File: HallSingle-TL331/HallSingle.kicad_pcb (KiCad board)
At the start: 2 copper layers, 12 x 23.5 mm, 11 parts, among them J1 Conn_01x03, U1 SS49E, U2 TL331

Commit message: Fixed TL orientation. ( previously fixed an error that was not an error ) thining is hard sometimes.
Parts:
- turned U2 to 0 degrees
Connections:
- U2 pad 1: Net-(C1-Pad1) -> Net-(U1-Pad2)
- U2 pad 3: Net-(U1-Pad2) -> Net-(C1-Pad1)
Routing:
- net Net-(U1-Pad2): track 5.80 -> 2.19 mm
- net Signal: track 32.7 -> 29.7 mm
- net GND: track 6.90 -> 4.70 mm
- net Net-(C1-Pad1): track 7.69 -> 6.98 mm
- net +5V: track 5.17 -> 4.62 mm, vias 3 -> 4
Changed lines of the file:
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@@
     (thickness 1.6)
     (drawings 12)
-    (tracks 58)
+    (tracks 55)
     (zones 0)
     (modules 11)
@@
   )
   (module Package_TO_SOT_SMD:SOT-23-5 (layer F.Cu)
-    (at 147.5 59.55 180)
+    (at 147.5 59.55)
     (descr "5-pin SOT23 package")
     (tags SOT-23-5)
@@
       (effects (font (size 0.5 0.5) (thickness 0.075)))
     )
-    (pad 5 smd rect (at 1.1 -0.95 180) (size 1.06 0.65) (layers F.Cu F.Paste F.Mask)
+    (pad 5 smd rect (at 1.1 -0.95) (size 1.06 0.65) (layers F.Cu F.Paste F.Mask)
       (net 3 +5V))
-    (pad 4 smd rect (at 1.1 0.95 180) (size 1.06 0.65) (layers F.Cu F.Paste F.Mask)
+    (pad 4 smd rect (at 1.1 0.95) (size 1.06 0.65) (layers F.Cu F.Paste F.Mask)
       (net 4 Signal))
-    (pad 3 smd rect (at -1.1 0.95 180) (size 1.06 0.65) (layers F.Cu F.Paste F.Mask)
+    (pad 3 smd rect (at -1.1 0.95) (size 1.06 0.65) (layers F.Cu F.Paste F.Mask)
+      (net 2 "Net-(C1-Pad1)"))
+    (pad 2 smd rect (at -1.1 0) (size 1.06 0.65) (layers F.Cu F.Paste F.Mask)
+      (net 1 GND))
+    (pad 1 smd rect (at -1.1 -0.95) (size 1.06 0.65) (layers F.Cu F.Paste F.Mask)
       (net 6 "Net-(U1-Pad2)"))
-    (pad 2 smd rect (at -1.1 0 180) (size 1.06 0.65) (layers F.Cu F.Paste F.Mask)
-      (net 1 GND))
-    (pad 1 smd rect (at -1.1 -0.95 180) (size 1.06 0.65) (layers F.Cu F.Paste F.Mask)
-      (net 2 "Net-(C1-Pad1)"))
     (model ${KISYS3DMOD}/Package_TO_SOT_SMD.3dshapes/SOT-23-5.wrl
       (at (xyz 0 0 0))
@@
   (gr_line (start 150 58) (end 150 79.5) (layer Edge.Cuts) (width 0.05))
   (gr_line (start 139 57) (end 149 57) (layer Edge.Cuts) (width 0.05))
+  (via (at 145.15 60.55) (size 0.8) (drill 0.4) (layers F.Cu B.Cu) (net 3))
   (segment (start 139.554001 58.946999) (end 139.954 58.547) (width 0.3048) (layer F.Cu) (net 1))
   (segment (start 142.272 59.5605) (end 142.272 59.5605) (width 0.6096) (layer F.Cu) (net 1))
   (segment (start 142.2825 59.55) (end 142.272 59.5605) (width 0.6096) (layer F.Cu) (net 1))
-  (segment (start 148.6 59.55) (end 142.2825 59.55) (width 0.6096) (layer F.Cu) (net 1))
+  (segment (start 146.4 59.55) (end 142.2825 59.55) (width 0.6096) (layer F.Cu) (net 1))
   (segment (start 148.45 62.725) (end 148.463 62.738) (width 0.3048) (layer F.Cu) (net 2))
   (segment (start 147.9885 62.738) (end 148.463 62.738) (width 0.3048) (layer F.Cu) (net 2))
@@
   (segment (start 148.463 62.45) (end 146.7485 62.45) (width 0.3048) (layer F.Cu) (net 2))
   (segment (start 146.558 64.9605) (end 146.558 62.9285) (width 0.3048) (layer F.Cu) (net 2))
+  (segment (start 148.463 60.637) (end 148.6 60.5) (width 0.3048) (layer F.Cu) (net 4))
+  (segment (start 148.6 62.2125) (end 148.45 62.3625) (width 0.3048) (layer F.Cu) (net 2))
   (segment (start 146.4 62.392) (end 146.558 62.55) (width 0.3048) (layer F.Cu) (net 2))
-  (segment (start 148.463 60.637) (end 148.6 60.5) (width 0.3048) (layer F.Cu) (net 2))
-  (segment (start 147.043527 62.064473) (end 146.558 62.55) (width 0.3048) (layer F.Cu) (net 2))
-  (segment (start 148.6 62.2125) (end 148.45 62.3625) (width 0.3048) (layer F.Cu) (net 2))
-  (segment (start 148.6 60.5) (end 148.6 62.2125) (width 0.3048) (layer F.Cu) (net 2))
+  (segment (start 146.4 60.5) (end 146.4 62.392) (width 0.3048) (layer F.Cu) (net 2))
   (via (at 142.15 63.5) (size 0.8) (drill 0.4) (layers F.Cu B.Cu) (net 3))
-  (via (at 145.25 61.05) (size 0.8) (drill 0.4) (layers F.Cu B.Cu) (net 3))
   (segment (start 139.446 62.738) (end 139.446 62.738) (width 0.6096) (layer F.Cu) (net 3))
   (segment (start 139.446 62.738) (end 139.7935 62.738) (width 0.6096) (layer F.Cu) (net 3))
@@
   (segment (start 141.65 63.95) (end 142.15 63.45) (width 0.6096) (layer F.Cu) (net 3))
   (segment (start 141.65 64.2375) (end 141.65 63.95) (width 0.6096) (layer F.Cu) (net 3))
-  (segment (start 145.8 60.5) (end 145.25 61.05) (width 0.6096) (layer F.Cu) (net 3))
-  (segment (start 146.4 60.5) (end 145.8 60.5) (width 0.6096) (layer F.Cu) (net 3))
-  (segment (start 144.7105 60.5105) (end 145.25 61.05) (width 0.6096) (layer F.Cu) (net 3))
-  (segment (start 144.272 60.5105) (end 144.7105 60.5105) (width 0.6096) (layer F.Cu) (net 3))
+  (via (at 147.7 58.05) (size 0.8) (drill 0.4) (layers F.Cu B.Cu) (net 3))
+  (segment (start 148.25 58.6) (end 147.7 58.05) (width 0.6096) (layer F.Cu) (net 3))
+  (segment (start 148.6 58.6) (end 148.25 58.6) (width 0.6096) (layer F.Cu) (net 3))
+  (segment (start 145.1105 60.5105) (end 145.15 60.55) (width 0.6096) (layer F.Cu) (net 3))
+  (segment (start 144.272 60.5105) (end 145.1105 60.5105) (width 0.6096) (layer F.Cu) (net 3))
   (via (at 140.9 61.4) (size 0.8) (drill 0.4) (layers F.Cu B.Cu) (net 4))
   (segment (start 141.65 62.15) (end 140.9 61.4) (width 0.3048) (layer F.Cu) (net 4))
@@
   (segment (start 140 60.5) (end 140.9 61.4) (width 0.3048) (layer F.Cu) (net 4))
   (segment (start 140 60.4375) (end 140 60.5) (width 0.3048) (layer F.Cu) (net 4))
+  (segment (start 148.6 60.5) (end 148.6 60.5) (width 0.3048) (layer F.Cu) (net 4))
+  (via (at 147.7 61.15) (size 0.8) (drill 0.4) (layers F.Cu B.Cu) (net 4))
+  (segment (start 148.35 60.5) (end 147.7 61.15) (width 0.3048) (layer F.Cu) (net 4))
+  (segment (start 148.6 60.5) (end 148.35 60.5) (width 0.3048) (layer F.Cu) (net 4))
+  (segment (start 149.4 62.85) (end 147.7 61.15) (width 0.3048) (layer B.Cu) (net 4))
+  (segment (start 149.399999 76.424291) (end 149.4 62.85) (width 0.3048) (layer B.Cu) (net 4))
+  (segment (start 148 78.58) (end 148 77.82429) (width 0.3048) (layer B.Cu) (net 4))
   (segment (start 148 77.82429) (end 149.399999 76.424291) (width 0.3048) (layer B.Cu) (net 4))
-  (segment (start 148 78.58) (end 148 77.82429) (width 0.3048) (layer B.Cu) (net 4))
-  (segment (start 146.451 58.6105) (end 146.4535 58.608) (width 0.3048) (layer F.Cu) (net 4))
-  (via (at 147.4 58.6) (size 0.8) (drill 0.4) (layers F.Cu B.Cu) (net 4))
-  (segment (start 146.4 58.6) (end 147.4 58.6) (width 0.3048) (layer F.Cu) (net 4))
-  (segment (start 149.399999 60.599999) (end 147.4 58.6) (width 0.3048) (layer B.Cu) (net 4))
-  (segment (start 149.399999 76.424291) (end 149.399999 60.599999) (width 0.3048) (layer B.Cu) (net 4))
-  (segment (start 141.299999 61.000001) (end 140.9 61.4) (width 0.3048) (layer B.Cu) (net 4))
-  (segment (start 146.255601 59.744399) (end 142.555601 59.744399) (width 0.3048) (layer B.Cu) (net 4))
-  (segment (start 142.555601 59.744399) (end 141.299999 61.000001) (width 0.3048) (layer B.Cu) (net 4))
-  (segment (start 147.4 58.6) (end 146.255601 59.744399) (width 0.3048) (layer B.Cu) (net 4))
+  (segment (start 147.300001 61.549999) (end 141.049999 61.549999) (width 0.3048) (layer B.Cu) (net 4))
+  (segment (start 141.049999 61.549999) (end 140.9 61.4) (width 0.3048) (layer B.Cu) (net 4))
+  (segment (start 147.7 61.15) (end 147.300001 61.549999) (width 0.3048) (layer B.Cu) (net 4))
+  (segment (start 146.451 58.6105) (end 146.4535 58.608) (width 0.3048) (layer F.Cu) (net 6))
   (segment (start 143.07763 74) (end 142 74) (width 0.3048) (layer F.Cu) (net 5))
   (segment (start 148.463 64.613) (end 146.794399 66.281601) (width 0.3048) (layer F.Cu) (net 5))
@@
   (segment (start 146.794399 70.283231) (end 143.07763 74) (width 0.3048) (layer F.Cu) (net 5))
   (segment (start 144.5 76.5) (end 142 74) (width 0.3048) (layer F.Cu) (net 5))
+  (segment (start 144.322 58.6105) (end 144.272 58.6105) (width 0.3048) (layer F.Cu) (net 6))
   (segment (start 144.2825 58.6) (end 144.272 58.6105) (width 0.3048) (layer F.Cu) (net 6))
-  (segment (start 144.322 58.6105) (end 144.272 58.6105) (width 0.3048) (layer F.Cu) (net 6))
-  (segment (start 144.272 57.9057) (end 144.272 58.6105) (width 0.3048) (layer F.Cu) (net 6))
-  (segment (start 148.474199 57.844399) (end 144.333301 57.844399) (width 0.3048) (layer F.Cu) (net 6))
-  (segment (start 148.6 57.9702) (end 148.474199 57.844399) (width 0.3048) (layer F.Cu) (net 6))
-  (segment (start 144.333301 57.844399) (end 144.272 57.9057) (width 0.3048) (layer F.Cu) (net 6))
-  (segment (start 148.6 58.6) (end 148.6 57.9702) (width 0.3048) (layer F.Cu) (net 6))
+  (segment (start 146.4 58.6) (end 144.2825 58.6) (width 0.3048) (layer F.Cu) (net 6))
   (zone (net 3) (net_name +5V) (layer B.Cu) (hatch edge 0.508)
     (connect_pads (clearance 0.508))

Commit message: added info to silkscreen
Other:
- board text added: "NC V1.1 TL331"
- board text removed: "NC V1.1"
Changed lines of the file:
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@@
     )
   )
-  (gr_text "NC V1.1\n" (at 139.15 69.05 90) (layer B.SilkS)
+  (gr_text "NC V1.1\nTL331" (at 139.9 69.1 90) (layer B.SilkS)
     (effects (font (size 1 1) (thickness 0.15)) (justify mirror))
   )
@@
   (gr_line (start 150 58) (end 150 79.5) (layer Edge.Cuts) (width 0.05))
   (gr_line (start 139 57) (end 149 57) (layer Edge.Cuts) (width 0.05))
-  (via (at 145.15 60.55) (size 0.8) (drill 0.4) (layers F.Cu B.Cu) (net 3))
   (segment (start 139.554001 58.946999) (end 139.954 58.547) (width 0.3048) (layer F.Cu) (net 1))
   (segment (start 142.272 59.5605) (end 142.272 59.5605) (width 0.6096) (layer F.Cu) (net 1))
@@
   (segment (start 148.463 62.45) (end 146.7485 62.45) (width 0.3048) (layer F.Cu) (net 2))
   (segment (start 146.558 64.9605) (end 146.558 62.9285) (width 0.3048) (layer F.Cu) (net 2))
-  (segment (start 148.463 60.637) (end 148.6 60.5) (width 0.3048) (layer F.Cu) (net 4))
   (segment (start 148.6 62.2125) (end 148.45 62.3625) (width 0.3048) (layer F.Cu) (net 2))
   (segment (start 146.4 62.392) (end 146.558 62.55) (width 0.3048) (layer F.Cu) (net 2))
   (segment (start 146.4 60.5) (end 146.4 62.392) (width 0.3048) (layer F.Cu) (net 2))
+  (via (at 145.15 60.55) (size 0.8) (drill 0.4) (layers F.Cu B.Cu) (net 3))
   (via (at 142.15 63.5) (size 0.8) (drill 0.4) (layers F.Cu B.Cu) (net 3))
   (segment (start 139.446 62.738) (end 139.446 62.738) (width 0.6096) (layer F.Cu) (net 3))
@@
   (segment (start 145.1105 60.5105) (end 145.15 60.55) (width 0.6096) (layer F.Cu) (net 3))
   (segment (start 144.272 60.5105) (end 145.1105 60.5105) (width 0.6096) (layer F.Cu) (net 3))
+  (segment (start 148.463 60.637) (end 148.6 60.5) (width 0.3048) (layer F.Cu) (net 4))
   (via (at 140.9 61.4) (size 0.8) (drill 0.4) (layers F.Cu B.Cu) (net 4))
   (segment (start 141.65 62.15) (end 140.9 61.4) (width 0.3048) (layer F.Cu) (net 4))
@@
   (segment (start 141.049999 61.549999) (end 140.9 61.4) (width 0.3048) (layer B.Cu) (net 4))
   (segment (start 147.7 61.15) (end 147.300001 61.549999) (width 0.3048) (layer B.Cu) (net 4))
-  (segment (start 146.451 58.6105) (end 146.4535 58.608) (width 0.3048) (layer F.Cu) (net 6))
   (segment (start 143.07763 74) (end 142 74) (width 0.3048) (layer F.Cu) (net 5))
   (segment (start 148.463 64.613) (end 146.794399 66.281601) (width 0.3048) (layer F.Cu) (net 5))
@@
   (segment (start 146.794399 70.283231) (end 143.07763 74) (width 0.3048) (layer F.Cu) (net 5))
   (segment (start 144.5 76.5) (end 142 74) (width 0.3048) (layer F.Cu) (net 5))
+  (segment (start 146.451 58.6105) (end 146.4535 58.608) (width 0.3048) (layer F.Cu) (net 6))
   (segment (start 144.322 58.6105) (end 144.272 58.6105) (width 0.3048) (layer F.Cu) (net 6))
   (segment (start 144.2825 58.6) (end 144.272 58.6105) (width 0.3048) (layer F.Cu) (net 6))

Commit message: further fixes and gerbers updated this time
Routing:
- net +5V: track 4.62 -> 4.96 mm, vias 4 -> 3
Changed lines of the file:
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@@
     (thickness 1.6)
     (drawings 12)
-    (tracks 55)
+    (tracks 52)
     (zones 0)
     (modules 11)
@@
   (gr_line (start 150 58) (end 150 79.5) (layer Edge.Cuts) (width 0.05))
   (gr_line (start 139 57) (end 149 57) (layer Edge.Cuts) (width 0.05))
+  (via (at 140.6 63.3) (size 0.8) (drill 0.4) (layers F.Cu B.Cu) (net 3))
   (segment (start 139.554001 58.946999) (end 139.954 58.547) (width 0.3048) (layer F.Cu) (net 1))
   (segment (start 142.272 59.5605) (end 142.272 59.5605) (width 0.6096) (layer F.Cu) (net 1))
@@
   (segment (start 146.4 60.5) (end 146.4 62.392) (width 0.3048) (layer F.Cu) (net 2))
   (via (at 145.15 60.55) (size 0.8) (drill 0.4) (layers F.Cu B.Cu) (net 3))
-  (via (at 142.15 63.5) (size 0.8) (drill 0.4) (layers F.Cu B.Cu) (net 3))
-  (segment (start 139.446 62.738) (end 139.446 62.738) (width 0.6096) (layer F.Cu) (net 3))
-  (segment (start 139.446 62.738) (end 139.7935 62.738) (width 0.6096) (layer F.Cu) (net 3))
-  (via (at 139.05 61.45) (size 0.8) (drill 0.4) (layers F.Cu B.Cu) (net 3))
-  (segment (start 139.6 62) (end 139.05 61.45) (width 0.6096) (layer F.Cu) (net 3))
-  (segment (start 139.6 62.3625) (end 139.6 62) (width 0.6096) (layer F.Cu) (net 3))
   (segment (start 141.65 64.2375) (end 141.6625 64.2375) (width 0.6096) (layer F.Cu) (net 3))
   (segment (start 148 73.5) (end 148 73.6) (width 0.3048) (layer B.Cu) (net 3))
-  (segment (start 141.65 63.95) (end 142.15 63.45) (width 0.6096) (layer F.Cu) (net 3))
-  (segment (start 141.65 64.2375) (end 141.65 63.95) (width 0.6096) (layer F.Cu) (net 3))
   (via (at 147.7 58.05) (size 0.8) (drill 0.4) (layers F.Cu B.Cu) (net 3))
   (segment (start 148.25 58.6) (end 147.7 58.05) (width 0.6096) (layer F.Cu) (net 3))
@@
   (segment (start 145.1105 60.5105) (end 145.15 60.55) (width 0.6096) (layer F.Cu) (net 3))
   (segment (start 144.272 60.5105) (end 145.1105 60.5105) (width 0.6096) (layer F.Cu) (net 3))
+  (segment (start 139.6625 62.3625) (end 140.6 63.3) (width 0.6096) (layer F.Cu) (net 3))
+  (segment (start 139.6 62.3625) (end 139.6625 62.3625) (width 0.6096) (layer F.Cu) (net 3))
+  (segment (start 141.5375 64.2375) (end 140.6 63.3) (width 0.6096) (layer F.Cu) (net 3))
+  (segment (start 141.65 64.2375) (end 141.5375 64.2375) (width 0.6096) (layer F.Cu) (net 3))
   (segment (start 148.463 60.637) (end 148.6 60.5) (width 0.3048) (layer F.Cu) (net 4))
   (via (at 140.9 61.4) (size 0.8) (drill 0.4) (layers F.Cu B.Cu) (net 4))

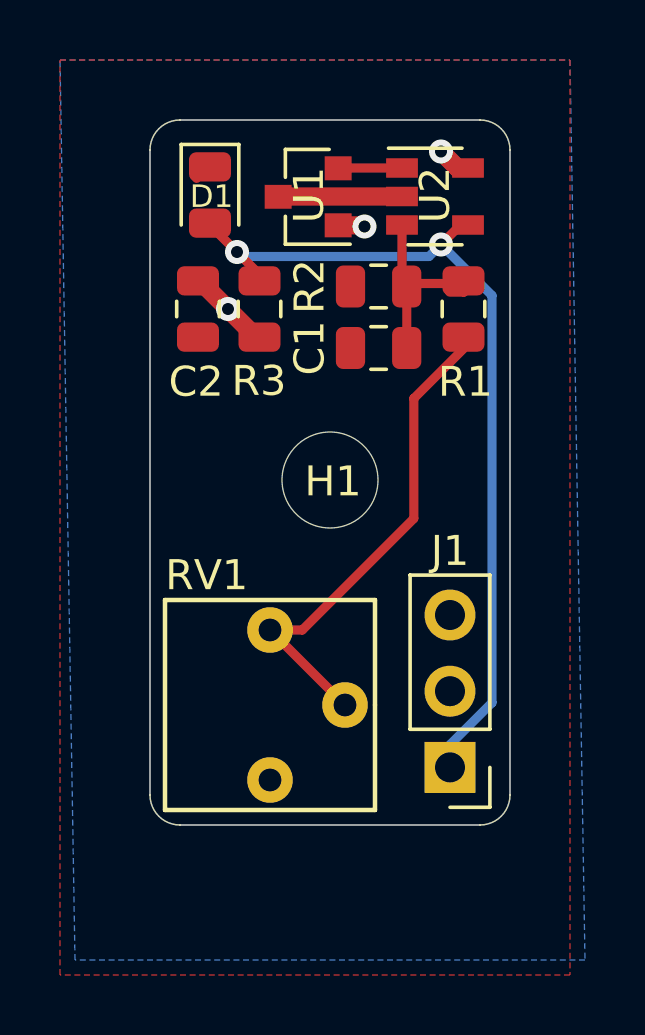
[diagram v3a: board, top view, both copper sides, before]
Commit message: Tinier components and different LED schematic
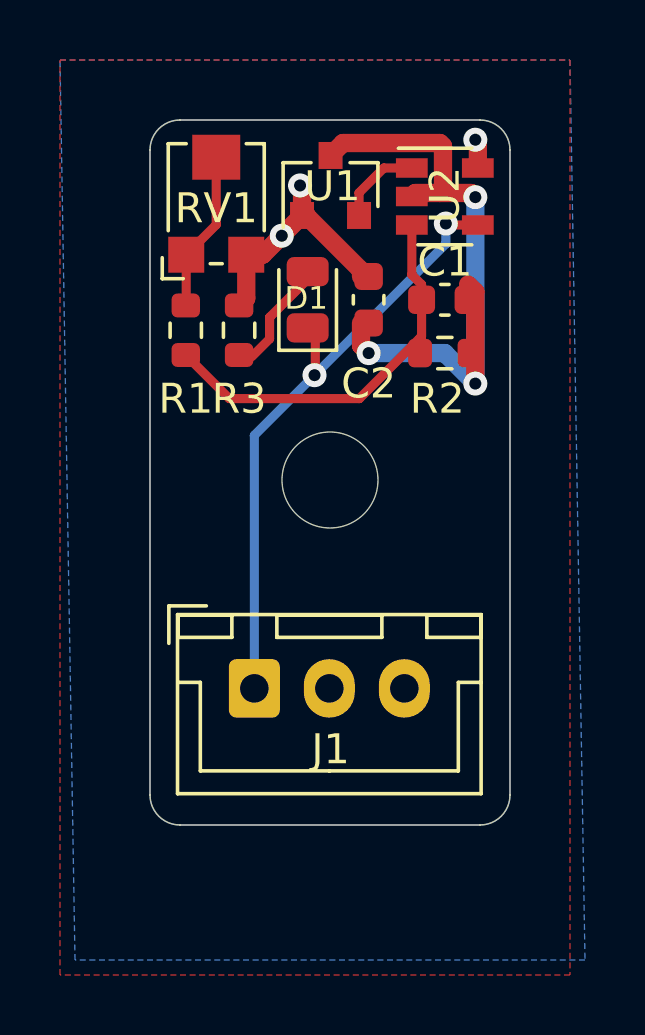
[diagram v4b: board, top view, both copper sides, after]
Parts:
- C1, C2: footprint HallEffect:C_0805_2012Metric -> Capacitor_SMD:C_0603_1608Metric
- J1: footprint HallEffect:PinHeader_1x03_P2.54mm_Vertical -> HallEffect:JST_XH_B3B-XH-A_1x03_P2.50mm_Vertical
- R1, R2, R3: footprint HallEffect:R_0805_2012Metric -> Resistor_SMD:R_0603_1608Metric
- RV1: footprint HallEffect:CT6EP103 -> HallEffect:Potentiometer_3x3
- moved RV1 16.9 mm to (140.2, 59.7), turned to 90 degrees
- moved R1 9.29 mm to (139.2, 64.0), turned to 270 degrees
- moved J1 7.03 mm to (141.5, 75.9), turned to 0 degrees
- moved C2 5.70 mm to (145.3, 63.0)
- moved D1 4.77 mm to (143.3, 63.0), turned to 90 degrees
- moved R2 3.13 mm to (147.8, 64.8), turned to 0 degrees
- moved C1 2.73 mm to (147.8, 63.0), turned to 0 degrees
- moved R3 0.98 mm to (141.0, 64.0), turned to 270 degrees
- moved U1 0.84 mm to (144.0, 59.2), turned to 90 degrees
- moved U2 0.33 mm to (147.8, 59.5)
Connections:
- D1 pad 1: GND -> Signal
- D1 pad 2: Signal -> Net-(D1-Pad2)
- R3 pad 2: Signal -> Net-(D1-Pad2)
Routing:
- net GND: track 4.70 -> 22.5 mm, vias 0 -> 3
- net Net-(R1-Pad1): track 16.2 -> 5.36 mm
- net Signal: track 29.7 -> 20.8 mm
- net Net-(C1-Pad1): track 6.98 -> 13.3 mm
- net +5V: track 4.96 -> 9.29 mm
- net Net-(D1-Pad2): track 0.00 -> 3.71 mm
- net Net-(U1-Pad2): track 2.19 -> 2.86 mm
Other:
- board text added: "NC V1.2 TL331"
- board text removed: "NC V1.1 TL331"

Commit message: Back to 0805 because it fits
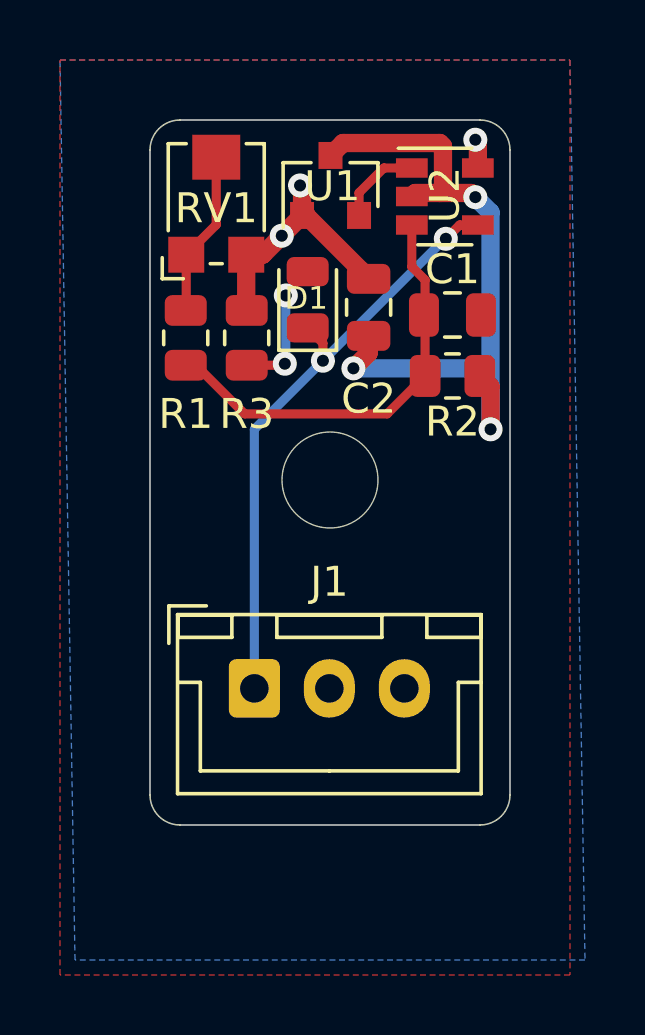
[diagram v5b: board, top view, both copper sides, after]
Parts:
- added REF**: OSHW-Symbol_6.7x6mm_SilkScreen, Symbol:OSHW-Symbol_6.7x6mm_SilkScreen, B.Cu at (144.0, 62.0)
- C1, C2: footprint Capacitor_SMD:C_0603_1608Metric -> Capacitor_SMD:C_0805_2012Metric
- J1: footprint HallEffect:JST_XH_B3B-XH-A_1x03_P2.50mm_Vertical -> Connector_JST:JST_XH_B3B-XH-A_1x03_P2.50mm_Vertical
- R1, R2, R3: footprint Resistor_SMD:R_0603_1608Metric -> Resistor_SMD:R_0805_2012Metric
- moved R2 0.80 mm to (148.1, 65.5)
- moved C1 0.57 mm to (148.1, 63.5)
- moved R3 0.36 mm to (141.2, 64.3)
- moved C2 0.25 mm to (145.3, 63.2)
- moved R1 0.25 mm to (139.2, 64.3)
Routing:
- net GND: track 22.5 -> 25.2 mm
- net Net-(C1-Pad1): track 13.3 -> 14.7 mm
- net Net-(D1-Pad2): track 3.71 -> 4.68 mm, vias 0 -> 2
- net Signal: track 20.8 -> 20.2 mm
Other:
- rule pad_to_mask_clearance: 0.051 -> 0
